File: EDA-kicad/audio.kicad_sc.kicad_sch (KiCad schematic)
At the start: 8 parts, among them J4 SJ2-35894B-SMT-TR, U3 CODEC-TLV320AIC3204IRHBR

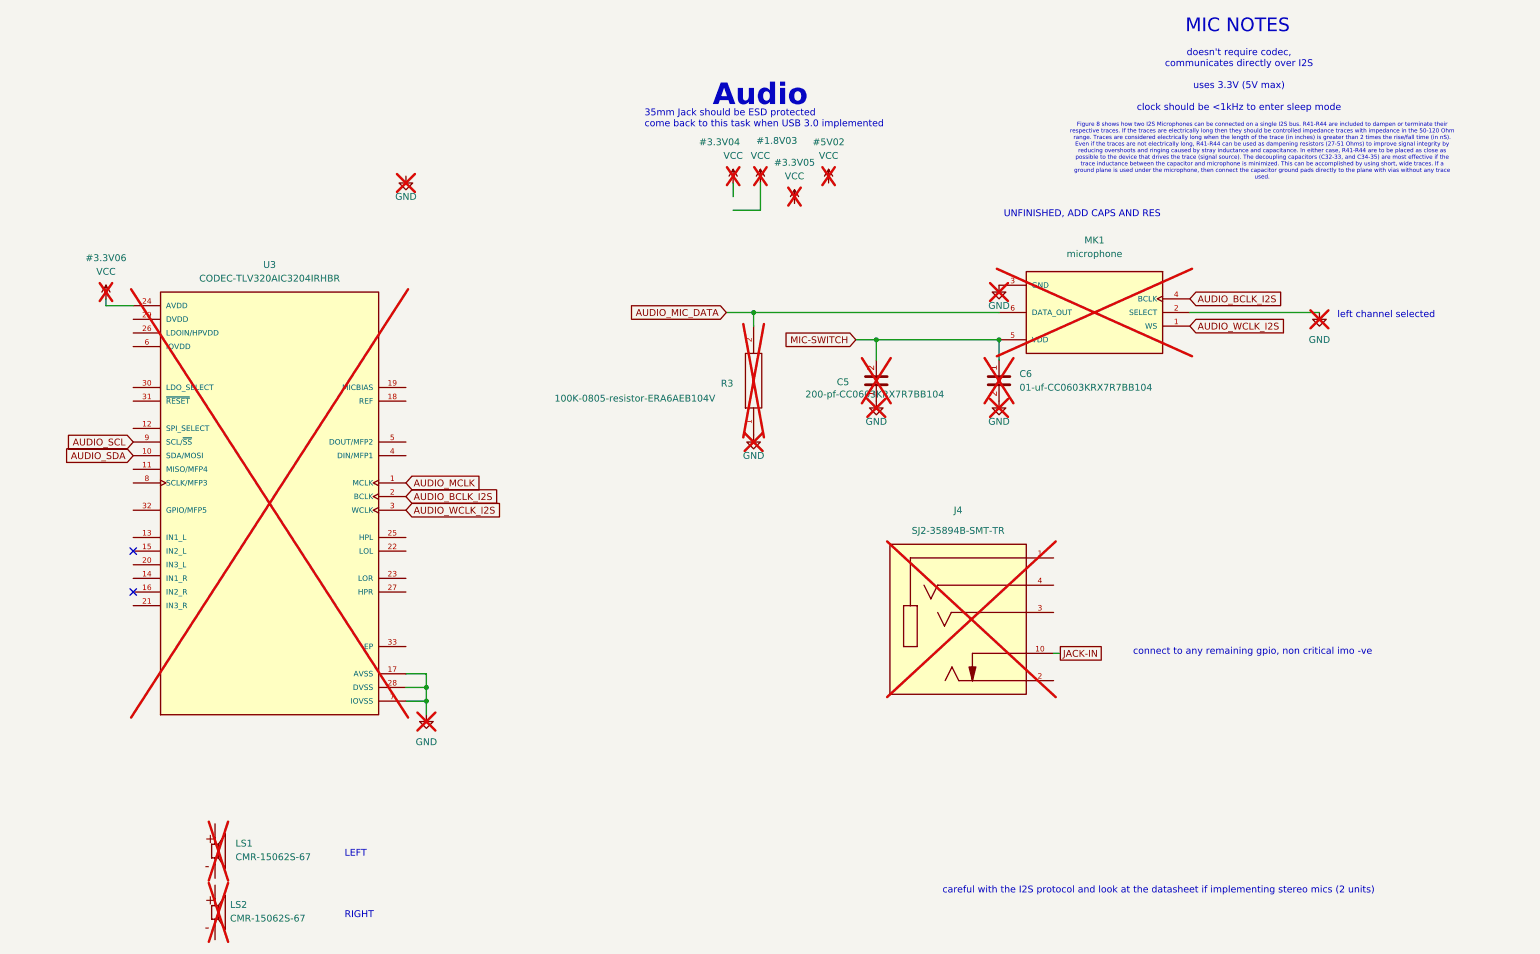
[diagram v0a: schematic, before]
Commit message: Improve KiCAD schematic design and labeling
- Replace overused global labels with hierarchical and local labels
- Add proper GND connections to components
- Fix BACKLIGHT- net issues
- Apply minor schematic fixes and cleanups
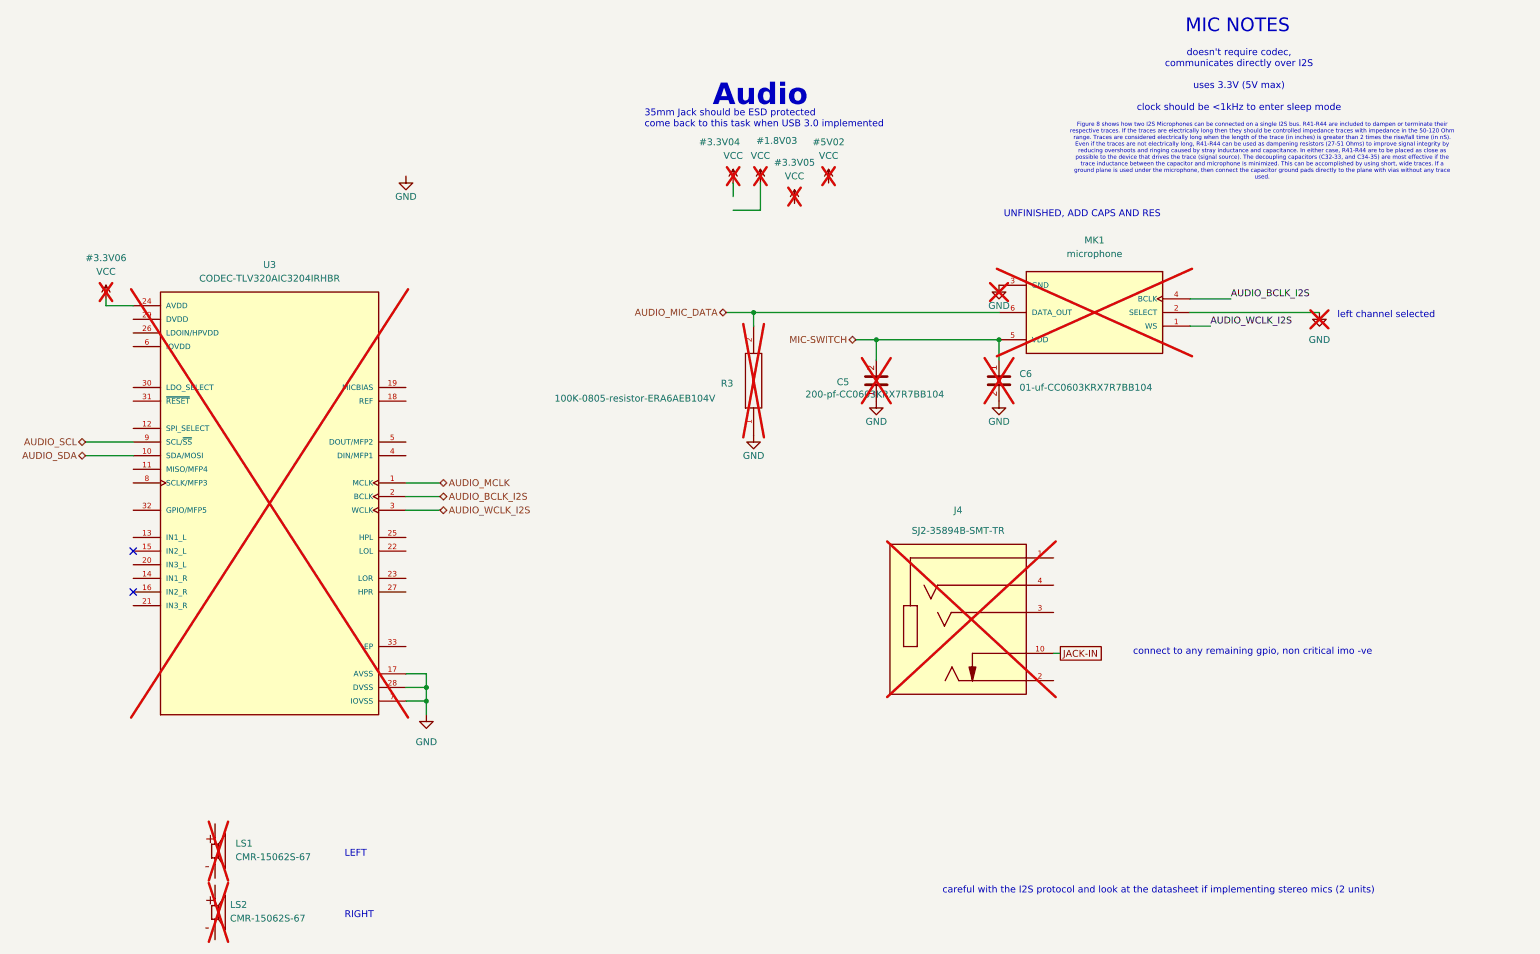
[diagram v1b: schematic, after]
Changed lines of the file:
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@@
+	(wire
+		(pts
+			(xy 85.09 92.71) (xy 91.44 92.71)
+		)
+		(stroke
+			(width 0)
+			(type default)
+		)
+	)
 	(wire
 		(pts
@@
 	(wire
 		(pts
+			(xy 238.76 58.42) (xy 231.14 58.42)
+		)
+		(stroke
+			(width 0)
+			(type default)
+		)
+	)
+	(wire
+		(pts
 			(xy 88.9 128.27) (xy 88.9 130.81)
 		)
@@
 	(wire
 		(pts
+			(xy 91.44 97.79) (xy 85.09 97.79)
+		)
+		(stroke
+			(width 0)
+			(type default)
+		)
+	)
+	(wire
+		(pts
 			(xy 151.13 36.83) (xy 151.13 41.91)
 		)
@@
 	(wire
 		(pts
+			(xy 25.4 87.63) (xy 34.29 87.63)
+		)
+		(stroke
+			(width 0)
+			(type default)
+		)
+	)
+	(wire
+		(pts
 			(xy 144.78 60.96) (xy 149.86 60.96)
 		)
@@
 	(wire
 		(pts
+			(xy 234.95 63.5) (xy 231.14 63.5)
+		)
+		(stroke
+			(width 0)
+			(type default)
+		)
+	)
+	(wire
+		(pts
 			(xy 172.72 69.85) (xy 172.72 66.04)
 		)
@@
 	(wire
 		(pts
+			(xy 85.09 95.25) (xy 91.44 95.25)
+		)
+		(stroke
+			(width 0)
+			(type default)
+		)
+	)
+	(wire
+		(pts
 			(xy 149.86 63.5) (xy 149.86 60.96)
 		)
@@
 		)
 	)
-	(global_label "AUDIO_BCLK_I2S"
-		(shape input)
-		(at 85.09 95.25 0)
-		(fields_autoplaced yes)
+	(wire
+		(pts
+			(xy 25.4 85.09) (xy 34.29 85.09)
+		)
+		(stroke
+			(width 0)
+			(type default)
+		)
+	)
+	(label "AUDIO_WCLK_I2S"
+		(at 234.95 63.5 0)
 		(effects
 			(font
 				(size 1.27 1.27)
 			)
-			(justify left)
-		)
-		(property "Intersheetrefs" "${INTERSHEET_REFS}"
-			(at 103.4967 95.25 0)
-			(effects
-				(font
-					(size 1.27 1.27)
-				)
-				(justify left)
-				(hide yes)
-			)
-		)
-	)
-	(global_label "AUDIO_WCLK_I2S"
-		(shape input)
-		(at 231.14 63.5 0)
-		(fields_autoplaced yes)
+			(justify left bottom)
+		)
+	)
+	(label "AUDIO_BCLK_I2S"
+		(at 238.76 58.42 0)
 		(effects
 			(font
 				(size 1.27 1.27)
 			)
-			(justify left)
-		)
-		(property "Intersheetrefs" "${INTERSHEET_REFS}"
-			(at 249.7281 63.5 0)
-			(effects
-				(font
-					(size 1.27 1.27)
-				)
-				(justify left)
-				(hide yes)
-			)
-		)
-	)
-	(global_label "AUDIO_SCL"
-		(shape input)
-		(at 34.29 85.09 180)
-		(fields_autoplaced yes)
-		(effects
-			(font
-				(size 1.27 1.27)
-			)
-			(justify right)
-		)
-		(property "Intersheetrefs" "${INTERSHEET_REFS}"
-			(at 21.2052 85.09 0)
-			(effects
-				(font
-					(size 1.27 1.27)
-				)
-				(justify right)
-				(hide yes)
-			)
-		)
-	)
-	(global_label "MIC-SWITCH"
-		(shape input)
-		(at 168.91 66.04 180)
-		(fields_autoplaced yes)
-		(effects
-			(font
-				(size 1.27 1.27)
-			)
-			(justify right)
-		)
-		(property "Intersheetrefs" "${INTERSHEET_REFS}"
-			(at 154.7645 65.9606 0)
-			(effects
-				(font
-					(size 1.27 1.27)
-				)
-				(justify right)
-				(hide yes)
-			)
-		)
-	)
-	(global_label "AUDIO_WCLK_I2S"
-		(shape input)
-		(at 85.09 97.79 0)
-		(fields_autoplaced yes)
-		(effects
-			(font
-				(size 1.27 1.27)
-			)
-			(justify left)
-		)
-		(property "Intersheetrefs" "${INTERSHEET_REFS}"
-			(at 103.6781 97.79 0)
-			(effects
-				(font
-					(size 1.27 1.27)
-				)
-				(justify left)
-				(hide yes)
-			)
-		)
-	)
-	(global_label "AUDIO_MIC_DATA"
-		(shape input)
-		(at 144.78 60.96 180)
-		(fields_autoplaced yes)
-		(effects
-			(font
-				(size 1.27 1.27)
-			)
-			(justify right)
-		)
-		(property "Intersheetrefs" "${INTERSHEET_REFS}"
-			(at 126.4942 60.96 0)
-			(effects
-				(font
-					(size 1.27 1.27)
-				)
-				(justify right)
-				(hide yes)
-			)
-		)
-	)
-	(global_label "AUDIO_BCLK_I2S"
-		(shape input)
-		(at 231.14 58.42 0)
-		(fields_autoplaced yes)
-		(effects
-			(font
-				(size 1.27 1.27)
-			)
-			(justify left)
-		)
-		(property "Intersheetrefs" "${INTERSHEET_REFS}"
-			(at 249.5467 58.42 0)
-			(effects
-				(font
-					(size 1.27 1.27)
-				)
-				(justify left)
-				(hide yes)
-			)
-		)
-	)
-	(global_label "AUDIO_MCLK"
-		(shape input)
-		(at 85.09 92.71 0)
-		(fields_autoplaced yes)
-		(effects
-			(font
-				(size 1.27 1.27)
-			)
-			(justify left)
-		)
-		(property "Intersheetrefs" "${INTERSHEET_REFS}"
-			(at 99.6867 92.71 0)
-			(effects
-				(font
-					(size 1.27 1.27)
-				)
-				(justify left)
-				(hide yes)
-			)
-		)
-	)
-	(global_label "AUDIO_SDA"
-		(shape input)
-		(at 34.29 87.63 180)
-		(fields_autoplaced yes)
-		(effects
-			(font
-				(size 1.27 1.27)
-			)
-			(justify right)
-		)
-		(property "Intersheetrefs" "${INTERSHEET_REFS}"
-			(at 21.1447 87.63 0)
-			(effects
-				(font
-					(size 1.27 1.27)
-				)
-				(justify right)
-				(hide yes)
-			)
+			(justify left bottom)
 		)
 	)
@@
 				(hide yes)
 			)
+		)
+	)
+	(hierarchical_label "AUDIO_MIC_DATA"
+		(shape bidirectional)
+		(at 144.78 60.96 180)
+		(effects
+			(font
+				(size 1.27 1.27)
+			)
+			(justify right)
+		)
+	)
+	(hierarchical_label "AUDIO_SDA"
+		(shape bidirectional)
+		(at 25.4 87.63 180)
+		(effects
+			(font
+				(size 1.27 1.27)
+			)
+			(justify right)
+		)
+	)
+	(hierarchical_label "AUDIO_SCL"
+		(shape bidirectional)
+		(at 25.4 85.09 180)
+		(effects
+			(font
+				(size 1.27 1.27)
+			)
+			(justify right)
+		)
+	)
+	(hierarchical_label "AUDIO_MCLK"
+		(shape bidirectional)
+		(at 91.44 92.71 0)
+		(effects
+			(font
+				(size 1.27 1.27)
+			)
+			(justify left)
+		)
+	)
+	(hierarchical_label "MIC-SWITCH"
+		(shape bidirectional)
+		(at 168.91 66.04 180)
+		(effects
+			(font
+				(size 1.27 1.27)
+			)
+			(justify right)
+		)
+	)
+	(hierarchical_label "AUDIO_BCLK_I2S"
+		(shape bidirectional)
+		(at 91.44 95.25 0)
+		(effects
+			(font
+				(size 1.27 1.27)
+			)
+			(justify left)
+		)
+	)
+	(hierarchical_label "AUDIO_WCLK_I2S"
+		(shape bidirectional)
+		(at 91.44 97.79 0)
+		(effects
+			(font
+				(size 1.27 1.27)
+			)
+			(justify left)
 		)
 	)
@@
 		(in_bom yes)
 		(on_board yes)
-		(dnp yes)
+		(dnp no)
 		(property "Reference" "#PWR070"
 			(at 195.58 83.82 0)
@@
 		(in_bom yes)
 		(on_board yes)
-		(dnp yes)
+		(dnp no)
 		(property "Reference" "#PWR069"
 			(at 172.72 83.82 0)
@@
 		(in_bom yes)
 		(on_board yes)
-		(dnp yes)
+		(dnp no)
 		(property "Reference" "#PWR066"
 			(at 85.09 41.91 0)
@@
 		(in_bom yes)
 		(on_board yes)
-		(dnp yes)
+		(dnp no)
 		(property "Reference" "#PWR071"
 			(at 149.86 90.17 0)
@@
 		(in_bom yes)
 		(on_board yes)
-		(dnp yes)
+		(dnp no)
 		(fields_autoplaced yes)
 		(property "Reference" "#PWR072"
